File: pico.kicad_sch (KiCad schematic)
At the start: 16 parts, among them J4 Conn_01x04_Pin, J6 Conn_01x05, J7 MEC1-110-02-F-D-A, U10 BMP581, U7 MCP23017x-x-ML, U9 DS3231MZ

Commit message: maj puissance
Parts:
- C9: footprint Capacitor_SMD:C_0603_1608Metric_Pad1.08x0.95mm_HandSolder -> Capacitor_SMD:C_0603_1608Metric
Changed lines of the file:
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@@
 		(property "Value" "Conn_01x04_Pin"
 			(at 143.51 139.7 90)
+			(hide yes)
 			(show_name no)
 			(do_not_autoplace no)
@@
 			)
 		)
-		(property "Footprint" "Capacitor_SMD:C_0603_1608Metric_Pad1.08x0.95mm_HandSolder"
+		(property "Footprint" "Capacitor_SMD:C_0603_1608Metric"
 			(at 101.6 165.1 0)
 			(hide yes)
@@
 		(property "Value" "Conn_01x05"
 			(at 74.93 130.8099 0)
-			(show_name no)
-			(do_not_autoplace no)
+			(hide yes)
+			(show_name no)
+			(do_not_autoplace no)

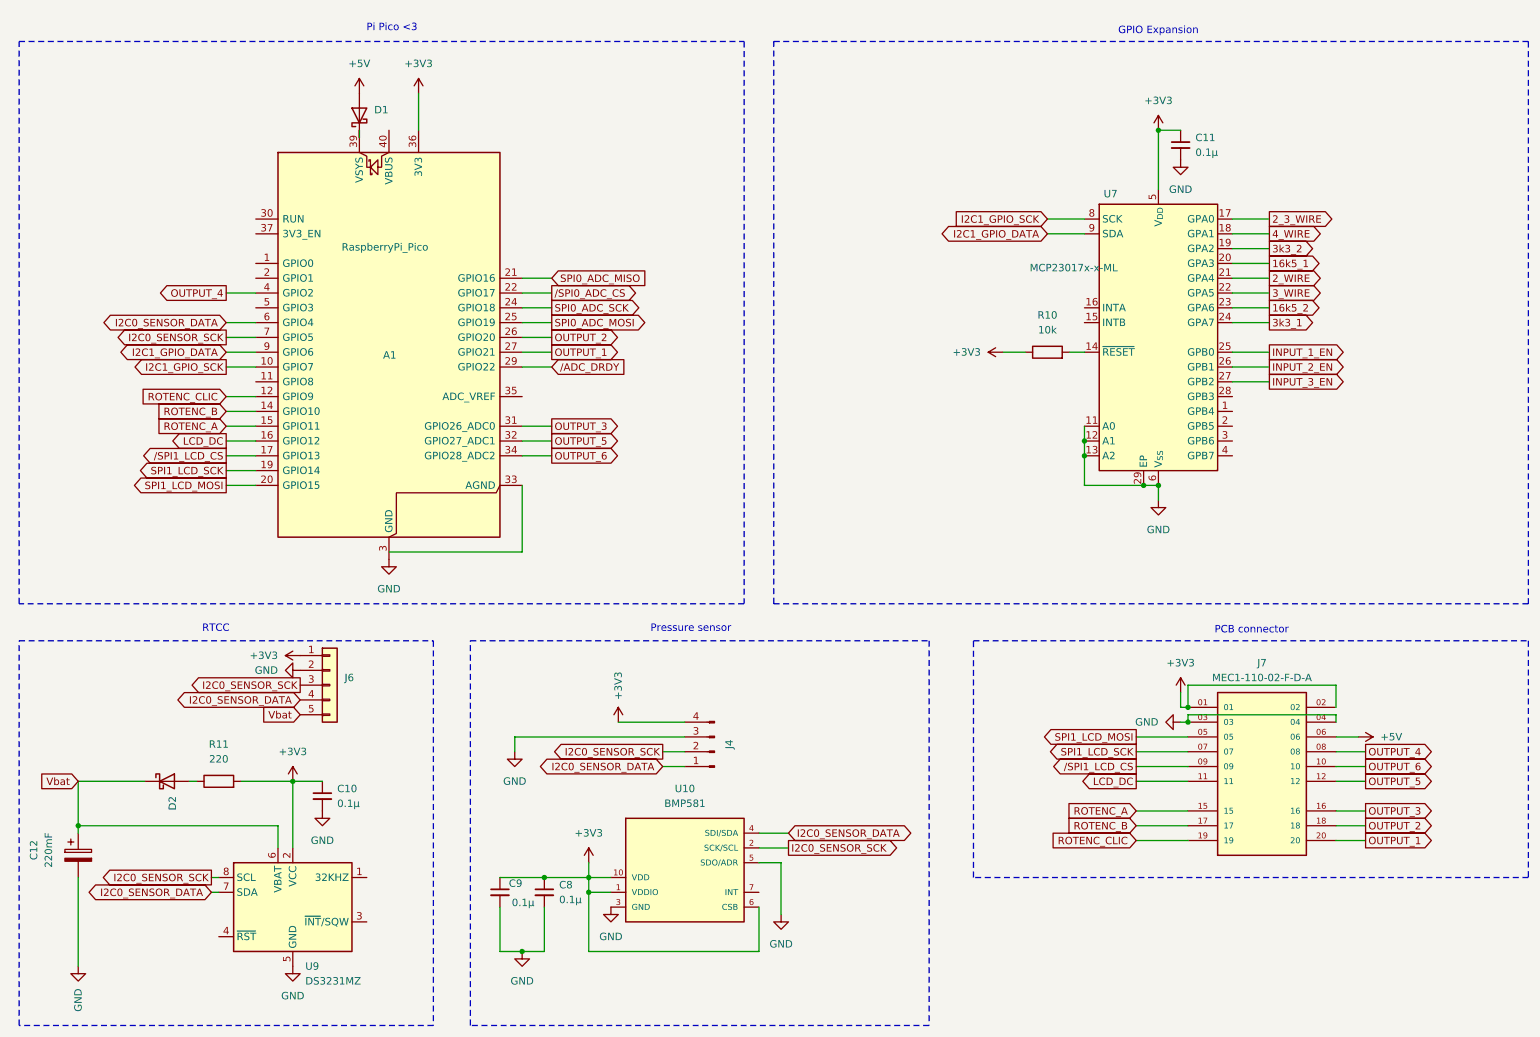
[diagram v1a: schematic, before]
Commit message: découpage et hierarchie
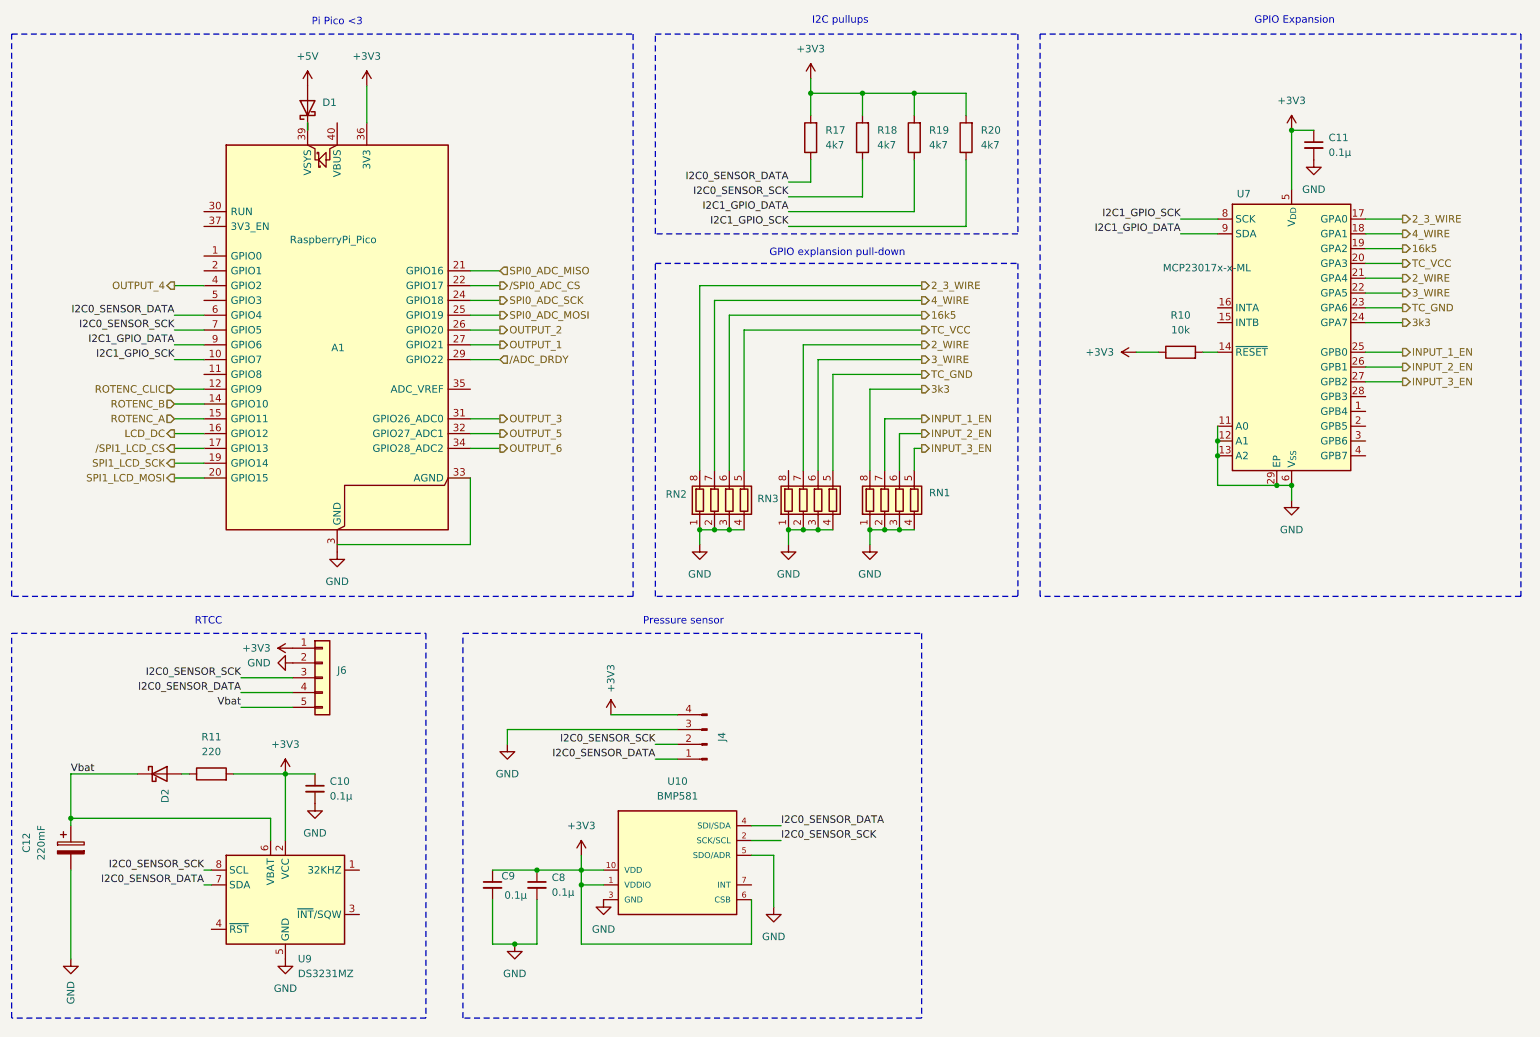
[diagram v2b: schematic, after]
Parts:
- removed J7: MEC1-110-02-F-D-A, OPC:MEC1-110-02-F-D-A-MALE, symbol OPC:MEC1-110-02-F-D-A
- added R17, R18, R19, R20: 4k7, Resistor_SMD:R_0603_1608Metric_Pad0.98x0.95mm_HandSolder, symbol Device:R
- added RN1, RN2, RN3: R_Pack04, Resistor_SMD:R_Array_Concave_4x0603, symbol Device:R_Pack04
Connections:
- net +3V3: now also R17.2, R18.2, R19.2, R20.2
- net 2_3_WIRE: now also RN2.8 (R1.2)
- net 2_WIRE: now also RN3.7 (R2.2)
- net 3_WIRE: now also RN3.6 (R3.2)
- net 4_WIRE: now also RN2.7 (R2.2)
- net GND: now also RN1.1 (R1.1), RN1.2 (R2.1), RN1.3 (R3.1), RN1.4 (R4.1), RN2.1 (R1.1), RN2.2 (R2.1), RN2.3 (R3.1), RN2.4 (R4.1), RN3.1 (R1.1), RN3.2 (R2.1), RN3.3 (R3.1), RN3.4 (R4.1)
- net I2C0_SENSOR_DATA: now also R17.1
- net I2C0_SENSOR_SCK: now also R18.1
- net I2C1_GPIO_DATA: now also R19.1
- net I2C1_GPIO_SCK: now also R20.1
- net INPUT_1_EN: now also RN1.7 (R2.2)
- net INPUT_2_EN: now also RN1.6 (R3.2)
- net INPUT_3_EN: now also RN1.5 (R4.2)
- net 16k5_1 renamed TC_VCC
- net TC_VCC: now also RN2.5 (R4.2)
- net 16k5_2 renamed TC_GND
- net TC_GND: now also RN3.5 (R4.2)
- net 3k3_1 renamed 3k3
- net 3k3: now also RN1.8 (R1.2)
- net 3k3_2 renamed 16k5
- net 16k5: now also RN2.6 (R3.2)
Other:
- note added: "GPIO explansion pull-down"
- note added: "I2C pullups"
- note removed: "PCB connector"

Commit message: update
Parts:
- RN1, RN2, RN3: value R_Pack04 -> 10k
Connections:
- net 16k5: no longer U7.19 (GPA2)
- net 3k3: now also RN1.5 (R4.2); no longer RN1.8 (R1.2), U7.24 (GPA7)
- net INPUT_1_EN: now also RN1.6 (R3.2); no longer RN1.7 (R2.2)
- net INPUT_2_EN: now also RN1.7 (R2.2); no longer RN1.6 (R3.2)
- net INPUT_3_EN: now also RN1.8 (R1.2); no longer RN1.5 (R4.2)
- new net RREF_16k5: U7.19 (GPA2)
- new net RREF_1k65: U7.24 (GPA7)
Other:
- moved on the sheet: RN1

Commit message: suite et nouvel écran
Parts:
- removed R19, R20: 4k7, Resistor_SMD:R_0603_1608Metric_Pad0.98x0.95mm_HandSolder, symbol Device:R
- D1: footprint Diode_SMD:D_SMA_Handsoldering -> Diode_SMD:D_SMA
- renumbered C12 to C1, C9 to C10, C8 to C12, C11 to C6, C10 to C9, J6 to J5, J4 to J6, R11 to R14, R18 to R15, R17 to R16, R10 to R9, RN3 to RN1, RN1 to RN2, RN2 to RN3, U7 to U3, U10 to U7, U9 to U8
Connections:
- net I2C1_GPIO_DATA is gone; now on net I2C1_DATA: A1.9 (GPIO6), U3.9 (SDA)
- net I2C1_GPIO_SCK is gone; now on net I2C1_SCK: A1.10 (GPIO7), U3.8 (SCK)
- net OUTPUT_4: now also A1.32 (GPIO27_ADC1); no longer A1.4 (GPIO2)
- net OUTPUT_5: now also A1.11 (GPIO8); no longer A1.32 (GPIO27_ADC1)
- net OUTPUT_6: now also A1.12 (GPIO9); no longer A1.34 (GPIO28_ADC2)
- net ROTENC_CLIC: now also A1.34 (GPIO28_ADC2); no longer A1.12 (GPIO9)
- net I2C0_SENSOR_DATA renamed I2C1_DATA
- net I2C1_DATA: no longer A1.6 (GPIO4)
- net I2C0_SENSOR_SCK renamed I2C1_SCK
- net I2C1_SCK: no longer A1.7 (GPIO5)
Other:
- note added: "I2C addr : 0x20"
- note added: "I2C addr : 0x46"
- note added: "I2C addr : 0x68"

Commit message: corrections
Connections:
- net 16k5 is gone; now on net RREF_16k5: RN3.6 (R3.2)
- net 3k3 is gone; now on net RREF_1k65: RN2.5 (R4.2)
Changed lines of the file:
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@@
-		)
-	)
-	(hierarchical_label "3k3"
-		(shape output)
-		(at 173.99 78.74 0)
-		(effects
-			(font
-				(size 1.27 1.27)
-			)
-			(justify left)
 		)
 	)
@@
 		)
 	)
-	(hierarchical_label "TC_VCC"
+	(hierarchical_label "RREF_1k65"
 		(shape output)
-		(at 173.99 68.58 0)
+		(at 173.99 78.74 0)
 		(effects
 			(font
@@
 		)
 	)
-	(hierarchical_label "16k5"
+	(hierarchical_label "TC_VCC"
 		(shape output)
-		(at 173.99 66.04 0)
+		(at 173.99 68.58 0)
 		(effects
 			(font
@@
 		(effects
 			(font
+				(size 1.27 1.27)
+			)
+			(justify left)
+		)
+	)
+	(hierarchical_label "RREF_16k5"
+		(shape output)
+		(at 173.99 66.04 0)
+		(effects
+			(font

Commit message: daily
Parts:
- A1: MPN (none) -> SC1631; px_x1 (none) -> 4,30
- C1: MPN (none) -> 3-158-695; px_x1 (none) -> 1.81; px_x10 (none) -> 1,62
- C10, C12, C6, C9: value 0.1µ -> 0.1µ 10V; MF (none) -> Würth Elektronik; MPN (none) -> 885012206020; px_x1 (none) -> 0,095; px_x10 (none) -> 0.031
- D1, D2: MF (none) -> Vishay; MPN (none) -> B140-E3/61T; px_x1 (none) -> 0,318; px_x10 (none) -> 0.195
- J5, J6: now left out of the parts list
- R14: MPN (none) -> ERJ-3GEYJ221V; px_x1 (none) -> 0,086; px_x10 (none) -> 0.02
- R15, R16: MF (none) -> Panasonic; MPN (none) -> ERJ-3GEYJ472V; px_x1 (none) -> 0.086; px_x10 (none) -> 0.02
- R9: MF (none) -> Panasonic; MPN (none) -> ERJ-3EKF1002V; px_x1 (none) -> 0,086; px_x10 (none) -> 0,021
- RN1, RN2, RN3: MF (none) -> Walsin; MPN (none) -> WA06X103JTL; px_x1 (none) -> 0,146; px_x10 (none) -> 0.092
- U3: MF (none) -> Microchip; MPN (none) -> MCP23017-E/ML; px_x1 (none) -> 1,58; px_x10 (none) -> 1,57
- U7: MPN (none) -> BMP581; px_x1 (none) -> 2,51; px_x10 (none) -> 2.24
- U8: MPN (none) -> DS3231MZ+TRL; px_x1 (none) -> 10.9; px_x10 (none) -> 8.57
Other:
- title: (none) -> Microcontroleur & GPIO

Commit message: daily
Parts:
- J5, J6: now in the parts list
- R12: renamed from R14; MF (none) -> Panasonic
- R13: renamed from R15; px_x1 0.086 -> 0,086
- R14: renamed from R16; px_x1 0.086 -> 0,086
- R2: renamed from R9; px_x10 0,021 -> 0.02
- RN1, RN2, RN3: px_x1 0,146 -> 0,086

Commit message: avant prod
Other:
- moved on the sheet: C10, C12, J6, U7
